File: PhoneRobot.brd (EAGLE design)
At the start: 50 x 50 mm, 52 parts, among them IC1 LP2985M5, K1 TX2-5V, K2 TX2-5V, K3 TX2-5V, K4 TX2-5V, K5 TX2-5V, Q1 2N3904SOT23, Q2 2N3904SOT23, Q3 2N3904SOT23, Q4 2N3904SOT23, Q5 2N3904SOT23, U1 G2XX3---PW20

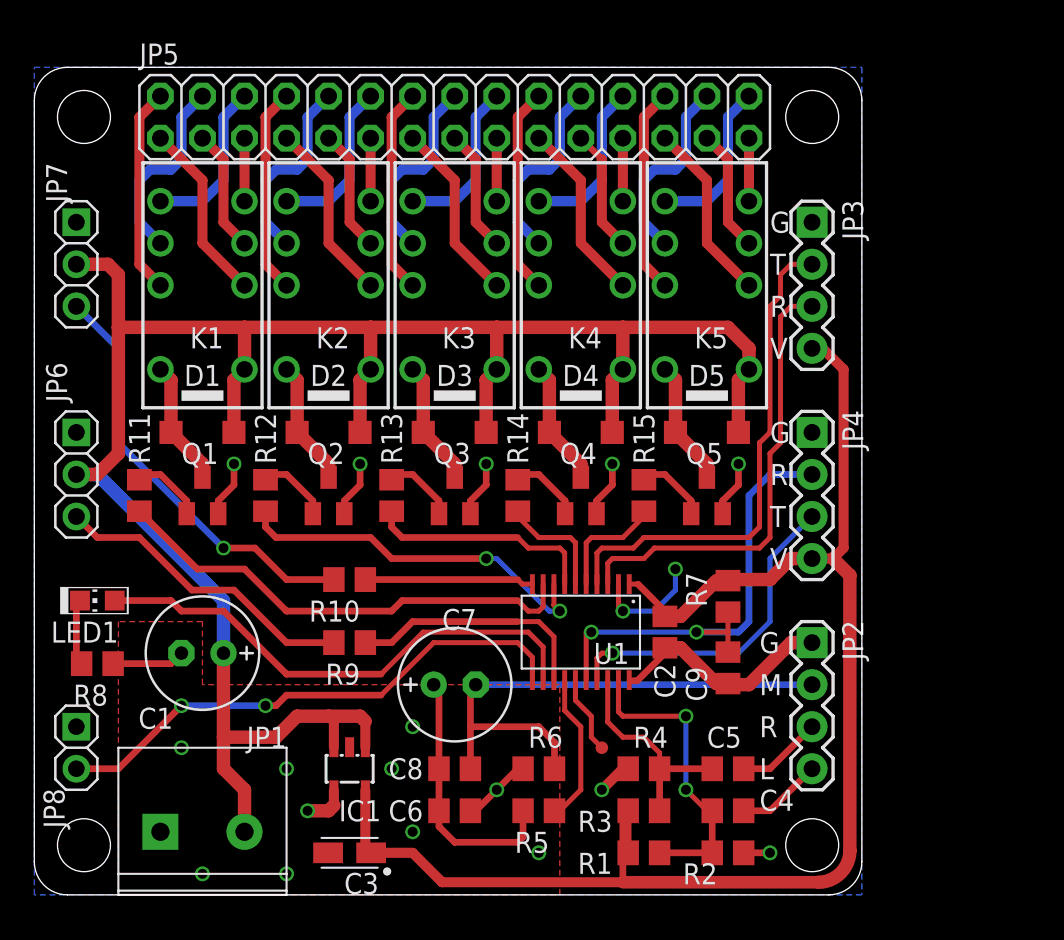
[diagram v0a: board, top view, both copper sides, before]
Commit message: Nominals changed after soldering first version
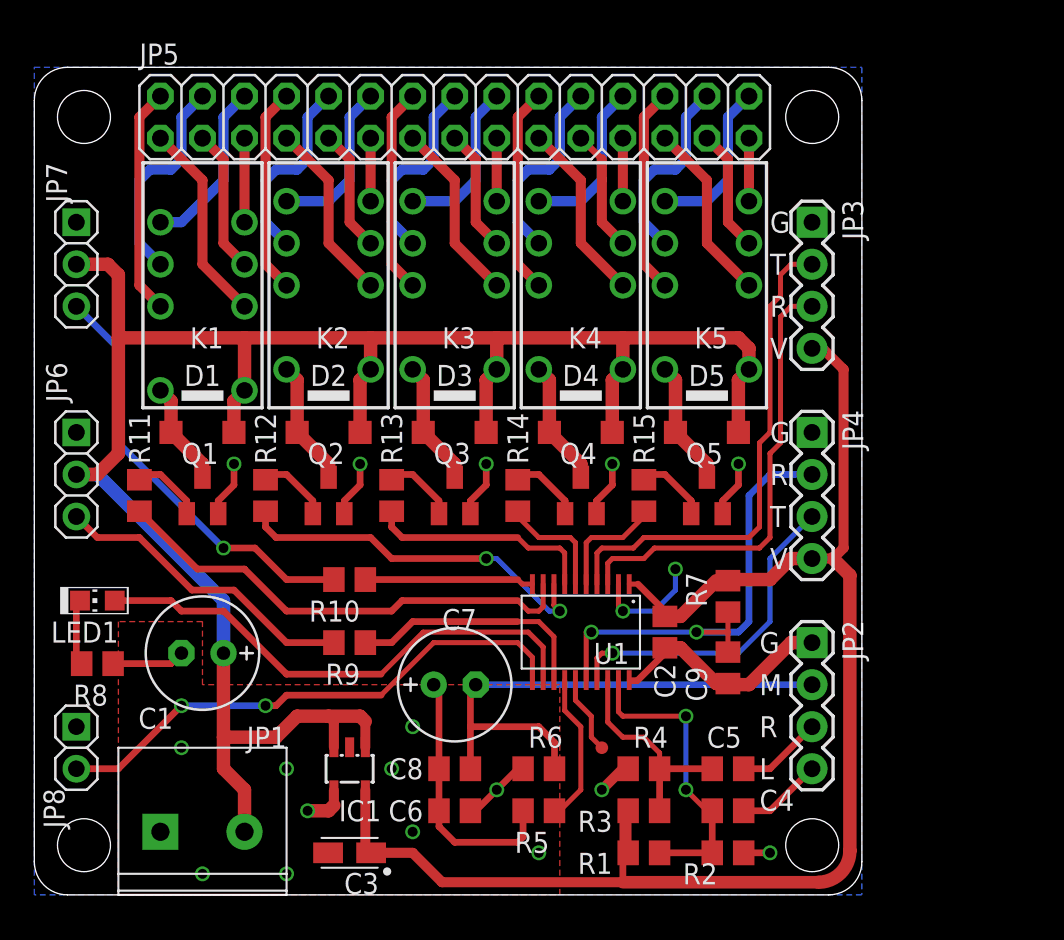
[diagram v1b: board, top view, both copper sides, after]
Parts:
- K1: value TX2-5V -> TXD2-5V; device relay:TX2 -> relay:TXD2
- R1, R2, R3, R4: value 10K -> 47K
- R11, R12, R13, R14, R15: value 4.7K -> 1K
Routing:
- net +5V: track 126.4 -> 123.6 mm
- net N$5: track 7.40 -> 8.67 mm
- net N$10: track 7.57 -> 6.30 mm
- net N$3: track 11.7 -> 13.0 mm
- net N$2: track 12.5 -> 13.8 mm
- net N$8: track 3.81 -> 5.08 mm
- net N$7: track 11.0 -> 12.3 mm
- net N$4: track 9.94 -> 10.5 mm

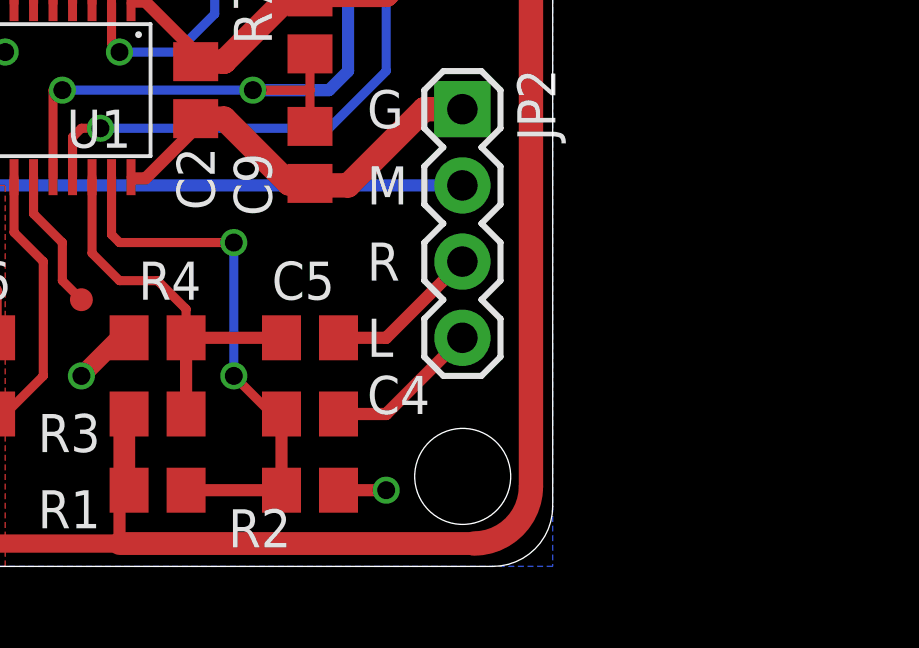
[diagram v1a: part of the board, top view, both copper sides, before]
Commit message: Fix Audio Input schematics
Schematics only, needs to fix layout
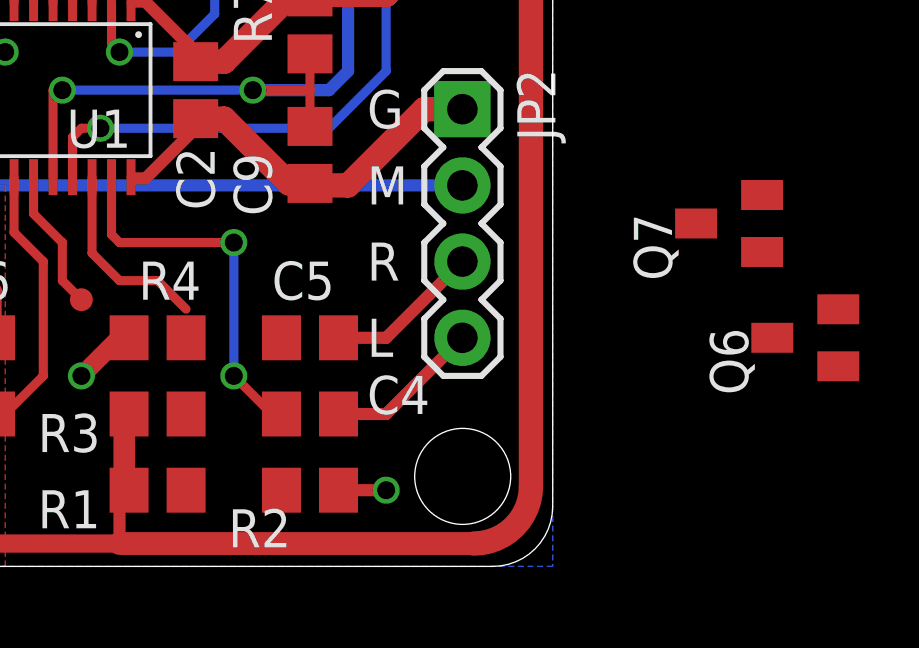
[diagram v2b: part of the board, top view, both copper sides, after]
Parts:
- added Q6, Q7: 2N3904SOT23, transistor-npn:SOT23-BEC
- C4, C5: value 2.2nf -> 100uf
- R2, R4: value 47K -> 10K
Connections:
- new net N$12: C4.2, Q6.B, R1.1, R2.2
- new net N$46: C5.2, Q7.B, R3.1, R4.2
- net GND: now also Q6.E, Q7.E
- net LEFT_D: now also Q6.C; no longer C4.2, R1.1, R2.2
- net RIGHT_D: now also Q7.C; no longer C5.2, R3.1, R4.2
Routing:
- net RIGHT_D: track 13.1 -> 6.44 mm
- net LEFT_D: track 18.4 -> 12.3 mm
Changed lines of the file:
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@@
 <attribute name="VALUE" x="37.465" y="5.08" size="1.27" layer="27" rot="R180"/>
 </element>
-<element name="R2" library="rcl" package="R0805" value="47K" x="41.91" y="2.54" locked="yes" smashed="yes" rot="R180">
+<element name="R2" library="rcl" package="R0805" value="10K" x="41.91" y="2.54" locked="yes" smashed="yes" rot="R180">
 <attribute name="NAME" x="41.275" y="1.905" size="1.27" layer="25" rot="R180"/>
 <attribute name="VALUE" x="42.545" y="5.08" size="1.27" layer="27" rot="R180"/>
 </element>
-<element name="C4" library="rcl" package="C0805" value="2.2nf" x="41.91" y="5.08" locked="yes" smashed="yes" rot="R180">
+<element name="C4" library="rcl" package="C0805" value="100uf" x="41.91" y="5.08" locked="yes" smashed="yes" rot="R180">
 <attribute name="NAME" x="43.815" y="5.08" size="1.27" layer="25"/>
 <attribute name="VALUE" x="43.18" y="7.62" size="1.27" layer="27" rot="R180"/>
@@
 <attribute name="VALUE" x="37.465" y="7.62" size="1.27" layer="27" rot="R180"/>
 </element>
-<element name="R4" library="rcl" package="R0805" value="47K" x="36.83" y="7.62" locked="yes"/>
-<element name="C5" library="rcl" package="C0805" value="2.2nf" x="41.91" y="7.62" locked="yes" smashed="yes" rot="R180">
+<element name="R4" library="rcl" package="R0805" value="10K" x="36.83" y="7.62" locked="yes"/>
+<element name="C5" library="rcl" package="C0805" value="100uf" x="41.91" y="7.62" locked="yes" smashed="yes" rot="R180">
 <attribute name="NAME" x="40.64" y="8.89" size="1.27" layer="25"/>
 <attribute name="VALUE" x="43.18" y="10.16" size="1.27" layer="27" rot="R180"/>
@@
 <attribute name="VALUE" x="10.795" y="33.02" size="1.27" layer="27" rot="R90"/>
 </element>
+<element name="Q6" library="transistor-npn" package="SOT23-BEC" value="2N3904SOT23" x="58.42" y="7.62" rot="R90"/>
+<element name="Q7" library="transistor-npn" package="SOT23-BEC" value="2N3904SOT23" x="55.88" y="11.43" rot="R90"/>
 </elements>
 <signals>
@@
 <via x="22.86" y="3.81" extent="1-16" drill="0.6"/>
 <via x="30.48" y="2.54" extent="1-16" drill="0.6"/>
+<contactref element="Q6" pad="E"/>
+<contactref element="Q7" pad="E"/>
+<wire x1="59.52" y1="8.57" x2="56.98" y2="12.38" width="0" layer="19" extent="1-1"/>
+<wire x1="10.16" y1="1.27" x2="59.52" y2="8.57" width="0" layer="19" extent="1-1"/>
 </signal>
 <signal name="RXD">
@@
 <wire x1="18.1" y1="10.475" x2="17.78" y2="10.795" width="0.6096" layer="1"/>
 <contactref element="K1" pad="1"/>
-<wire x1="12.7" y1="30.48" x2="12.7" y2="3.81" width="0" layer="19" extent="1-1"/>
 </signal>
 <signal name="+3V3" class="2">
@@
 </signal>
 <signal name="LEFT_D">
-<contactref element="C4" pad="2"/>
-<contactref element="R1" pad="1"/>
-<contactref element="R2" pad="2"/>
 <contactref element="U1" pad="19"/>
-<wire x1="40.96" y1="5.08" x2="40.96" y2="2.54" width="0.4064" layer="1"/>
-<wire x1="40.96" y1="2.54" x2="37.78" y2="2.54" width="0.4064" layer="1"/>
 <wire x1="35.2949" y1="12.975" x2="35.2949" y2="11.0601" width="0.3048" layer="1"/>
 <wire x1="35.2949" y1="11.0601" x2="35.56" y2="10.795" width="0.3048" layer="1"/>
@@
 <via x="39.37" y="6.35" extent="1-16" drill="0.6"/>
 <wire x1="39.37" y1="6.35" x2="40.64" y2="5.08" width="0.3048" layer="1"/>
-<wire x1="40.64" y1="5.08" x2="40.96" y2="5.08" width="0.3048" layer="1"/>
+<contactref element="Q6" pad="C"/>
+<wire x1="57.32" y1="7.62" x2="35.2949" y2="11.0601" width="0" layer="19" extent="1-1"/>
 </signal>
 <signal name="LEFT_A">
@@
 </signal>
 <signal name="RIGHT_D">
-<contactref element="C5" pad="2"/>
-<contactref element="R3" pad="1"/>
-<contactref element="R4" pad="2"/>
 <contactref element="U1" pad="18"/>
-<wire x1="40.96" y1="7.62" x2="37.78" y2="7.62" width="0.4064" layer="1"/>
-<wire x1="37.78" y1="7.62" x2="37.78" y2="5.08" width="0.4064" layer="1"/>
 <wire x1="34.645" y1="12.975" x2="34.645" y2="10.44" width="0.3048" layer="1"/>
 <wire x1="34.645" y1="10.44" x2="35.56" y2="9.525" width="0.3048" layer="1"/>
 <wire x1="35.56" y1="9.525" x2="36.83" y2="9.525" width="0.3048" layer="1"/>
 <wire x1="36.83" y1="9.525" x2="37.78" y2="8.575" width="0.3048" layer="1"/>
-<wire x1="37.78" y1="8.575" x2="37.78" y2="7.62" width="0.3048" layer="1"/>
+<contactref element="Q7" pad="C"/>
+<wire x1="54.78" y1="11.43" x2="34.645" y2="10.44" width="0" layer="19" extent="1-1"/>
 </signal>
 <signal name="N$1">
@@
 <wire x1="17.78" y1="5.08" x2="16.51" y2="5.08" width="0.8128" layer="1"/>
 </signal>
+<signal name="N$12">
+<contactref element="C4" pad="2"/>
+<contactref element="Q6" pad="B"/>
+<contactref element="R2" pad="2"/>
+<contactref element="R1" pad="1"/>
+<wire x1="40.96" y1="2.54" x2="40.96" y2="5.08" width="0" layer="19" extent="1-1"/>
+<wire x1="37.78" y1="2.54" x2="40.96" y2="2.54" width="0" layer="19" extent="1-1"/>
+<wire x1="59.52" y1="6.67" x2="37.78" y2="2.54" width="0" layer="19" extent="1-1"/>
+</signal>
+<signal name="N$46">
+<contactref element="C5" pad="2"/>
+<contactref element="R4" pad="2"/>
+<contactref element="R3" pad="1"/>
+<contactref element="Q7" pad="B"/>
+<wire x1="37.78" y1="7.62" x2="40.96" y2="7.62" width="0" layer="19" extent="1-1"/>
+<wire x1="37.78" y1="5.08" x2="37.78" y2="7.62" width="0" layer="19" extent="1-1"/>
+<wire x1="56.98" y1="10.48" x2="37.78" y2="5.08" width="0" layer="19" extent="1-1"/>
+</signal>
 </signals>
